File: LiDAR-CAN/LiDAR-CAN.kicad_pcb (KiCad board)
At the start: 4 copper layers, 60 x 55 mm, 138 parts, among them J1 XT30(2+2), J2 XT30(2+2), J3 G7LX-A88S7-BP-G/Y, J4 XT30(2+2), J5 61300511121, SW1 RST, U1 LMR51430, U2 LMR51430, U3 W5500, U4 TCAN4550RGY, U5 STM32F401RBT6, Y1 25MHz, Y2 40MHz, Y3 25MHz

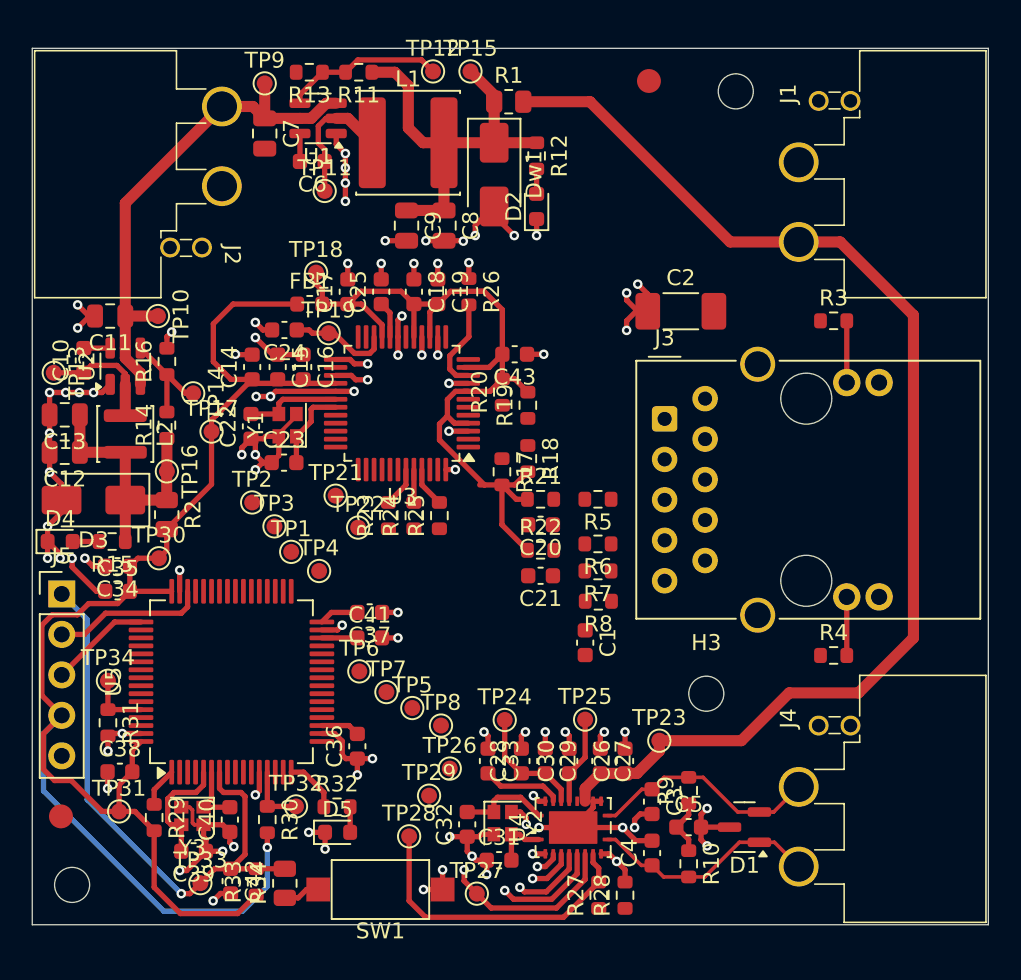
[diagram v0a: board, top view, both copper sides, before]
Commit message: Add Ethernet connector routing
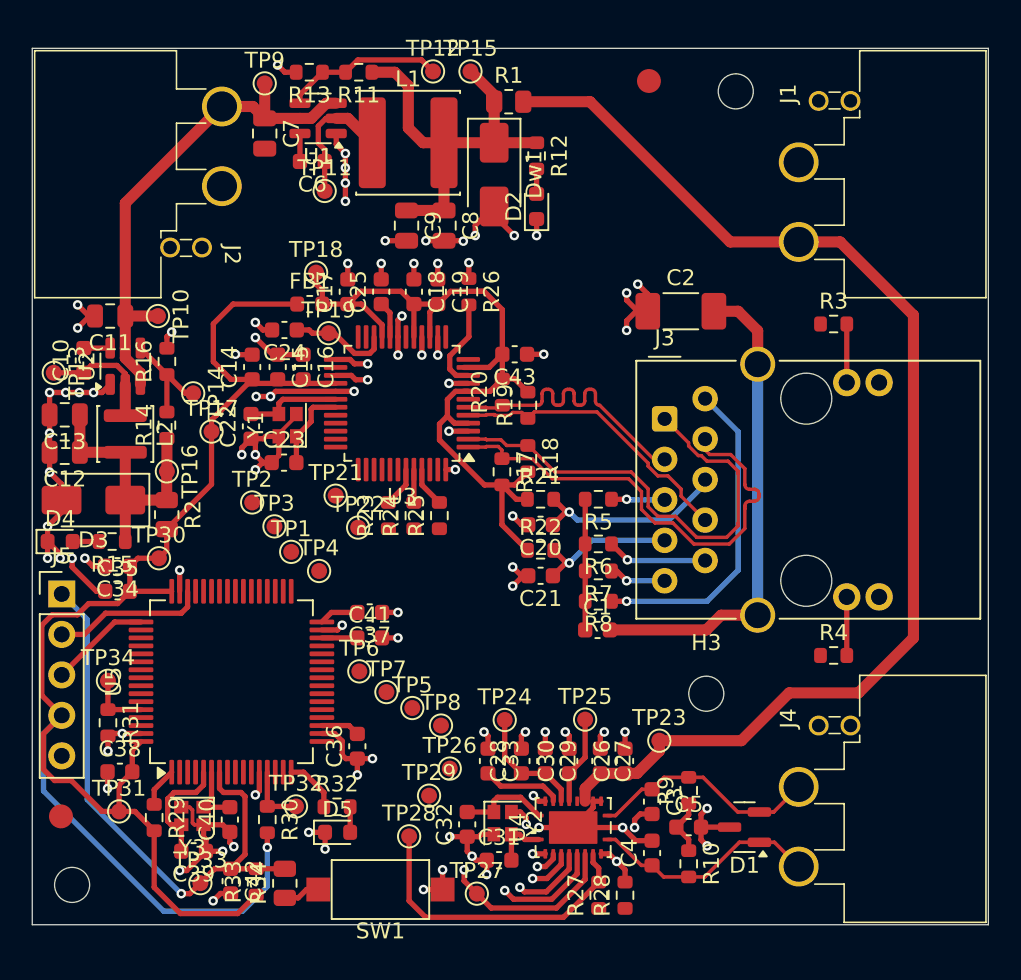
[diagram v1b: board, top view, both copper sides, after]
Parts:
- moved C1 1.11 mm to (155.5, 101.5), turned to 0 degrees
- moved R3 0.20 mm to (170.3, 82.3)
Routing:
- net CHASSIS_GND: track 0.00 -> 30.8 mm
- net /LiDAR Interface/TXP: track 0.00 -> 30.0 mm
- net /LiDAR Interface/TXN: track 0.00 -> 29.9 mm
- net Net-(J3-R4): track 0.00 -> 20.4 mm, vias 0 -> 1
- net /LiDAR Interface/RXN: track 0.00 -> 18.5 mm
- net /LiDAR Interface/RXP: track 0.00 -> 18.3 mm
- net /LiDAR Interface/TCT: track 0.00 -> 12.6 mm, vias 0 -> 1
- net /LiDAR Interface/RCT: track 0.00 -> 9.24 mm, vias 0 -> 1
- net Net-(C1-Pad1): track 0.00 -> 8.23 mm
- net Net-(J3-R2): track 0.00 -> 6.31 mm, vias 0 -> 1
- net GND: track 143.2 -> 148.2 mm, vias 82 -> 86
- net Net-(J3-R3): track 0.00 -> 3.59 mm, vias 0 -> 1
- net Net-(J3-R1): track 0.00 -> 3.35 mm, vias 0 -> 1

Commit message: Add SPI buses routing
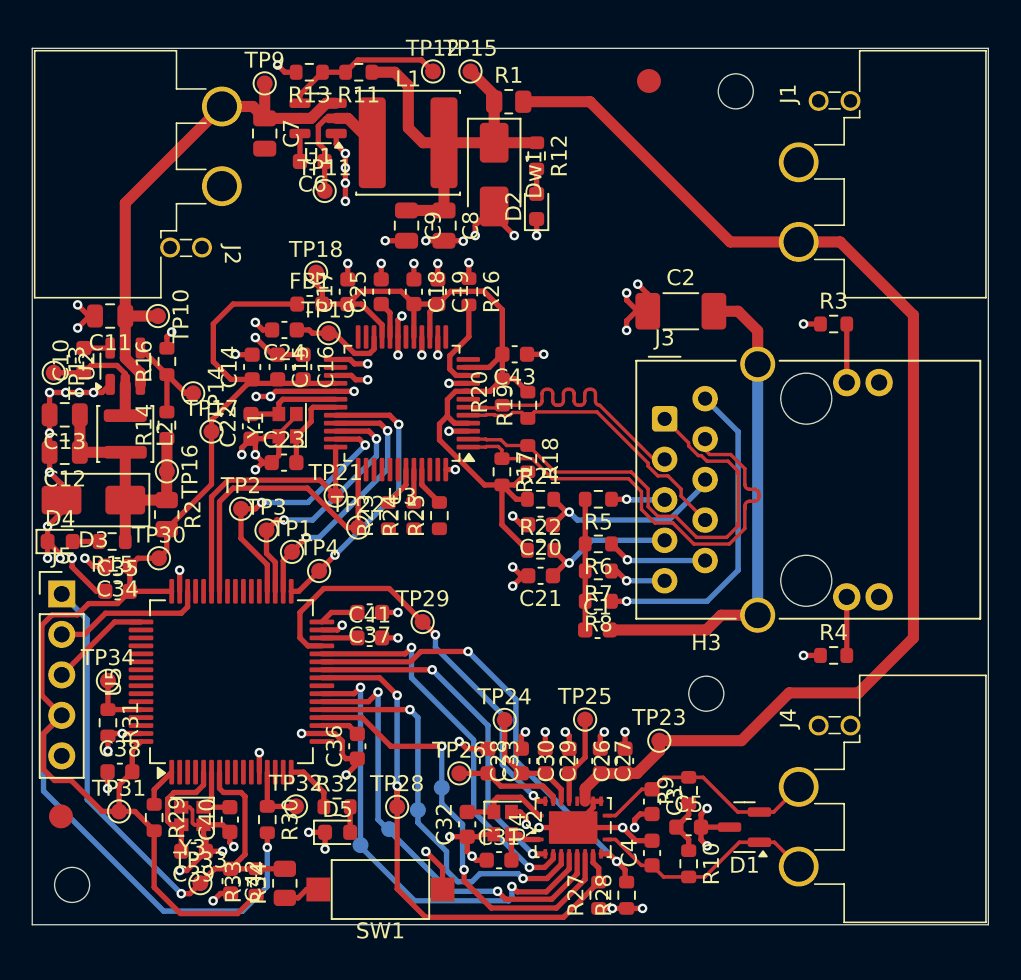
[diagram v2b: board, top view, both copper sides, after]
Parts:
- removed TP27: TestPoint, TestPoint:TestPoint_Pad_D1.0mm
- TP5, TP6, TP7, TP8: moved to B.Cu
- moved TP29 10.9 mm to (144.5, 101.0)
- moved TP6 10.9 mm to (140.6, 115.0), turned to 180 degrees
- moved TP7 8.60 mm to (142.4, 114.0), turned to 180 degrees
- moved TP5 6.41 mm to (144.2, 112.8), turned to 180 degrees
- moved TP8 3.90 mm to (145.7, 111.4), turned to 180 degrees
- moved TP28 2.00 mm to (142.9, 112.6)
- moved TP2 0.81 mm to (133.1, 93.9)
- moved TP26 0.67 mm to (146.8, 110.5)
- moved TP3 0.56 mm to (134.7, 95.2)
- moved R28 0.10 mm to (157.3, 118.2)
- moved TP1 0.05 mm to (136.3, 96.6)
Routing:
- net /CAN Interface/GPIO2: track 2.69 -> 29.2 mm, vias 1 -> 2
- net /CAN Interface/RST: track 0.89 -> 27.0 mm, vias 1 -> 2
- net /CAN Interface/SDI: track 4.76 -> 29.6 mm, vias 1 -> 2
- net /CAN Interface/GPIO1: track 1.51 -> 24.7 mm, vias 1 -> 2
- net /CAN Interface/SCLK: track 2.82 -> 25.4 mm, vias 1 -> 2
- net /CAN Interface/SDO: track 6.69 -> 28.3 mm, vias 1 -> 2
- net /CAN Interface/~{WKRQ}: track 0.79 -> 21.9 mm, vias 1 -> 2
- net /LiDAR Interface/~{RST}: track 0.00 -> 19.3 mm
- net /LiDAR Interface/~{SCS}: track 0.00 -> 17.7 mm, vias 0 -> 2
- net /LiDAR Interface/~{INT}: track 0.00 -> 17.6 mm
- net /LiDAR Interface/MOSI: track 0.00 -> 17.3 mm, vias 0 -> 2
- net /LiDAR Interface/MISO: track 0.00 -> 16.7 mm, vias 0 -> 2
- net /LiDAR Interface/SCLK: track 0.00 -> 16.7 mm, vias 0 -> 2
- net /CAN Interface/~{CS}: track 11.3 -> 27.9 mm, vias 1 -> 2
- net /CAN Interface/~{INT}: track 19.2 -> 34.9 mm, vias 0 -> 2
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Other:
- board text added: "FABRICATION DRAWING"

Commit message: Complete routing and all nets
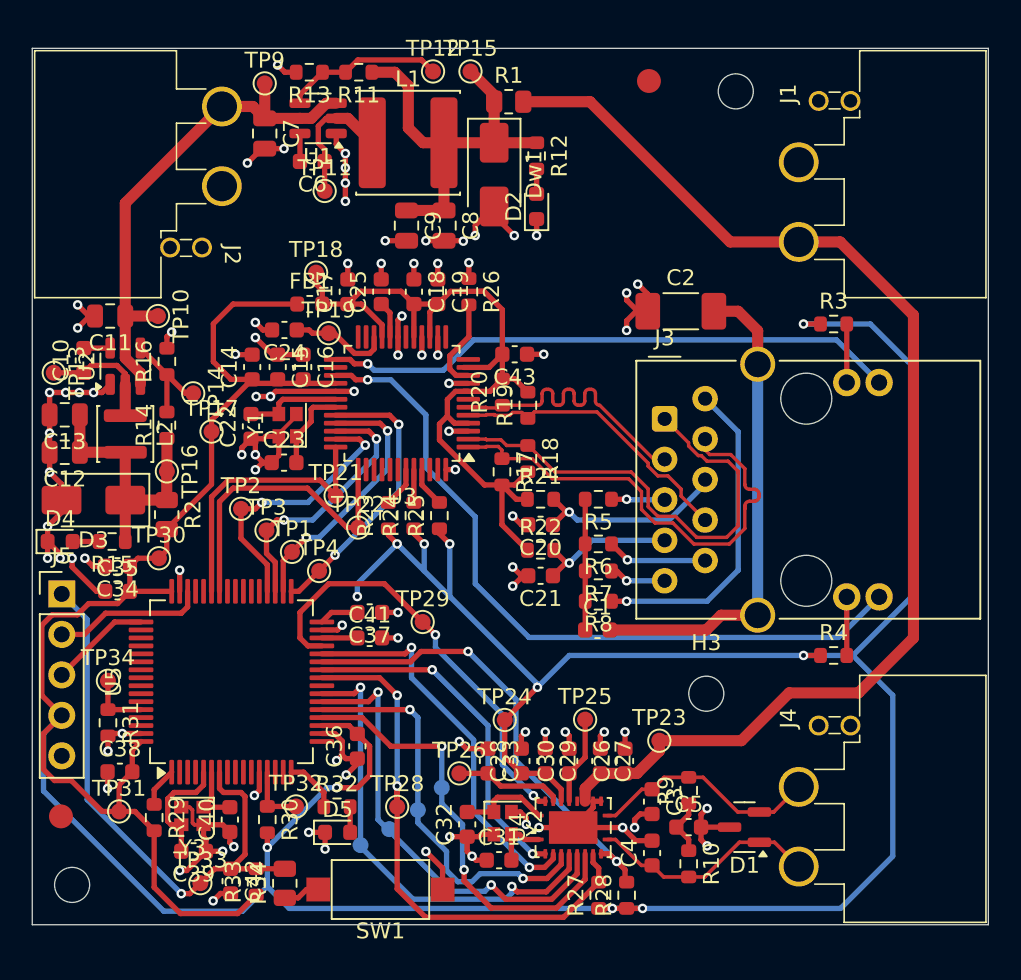
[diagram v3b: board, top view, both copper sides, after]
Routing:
- net +3.3V: track 120.4 -> 263.3 mm, vias 5 -> 11
- net /LiDAR Interface/ACTLED: track 2.13 -> 46.4 mm
- net /LiDAR Interface/LINKLED: track 2.13 -> 36.3 mm
- net GND: track 148.8 -> 151.4 mm, vias 84 -> 86

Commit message: Add new silkscreen annotation
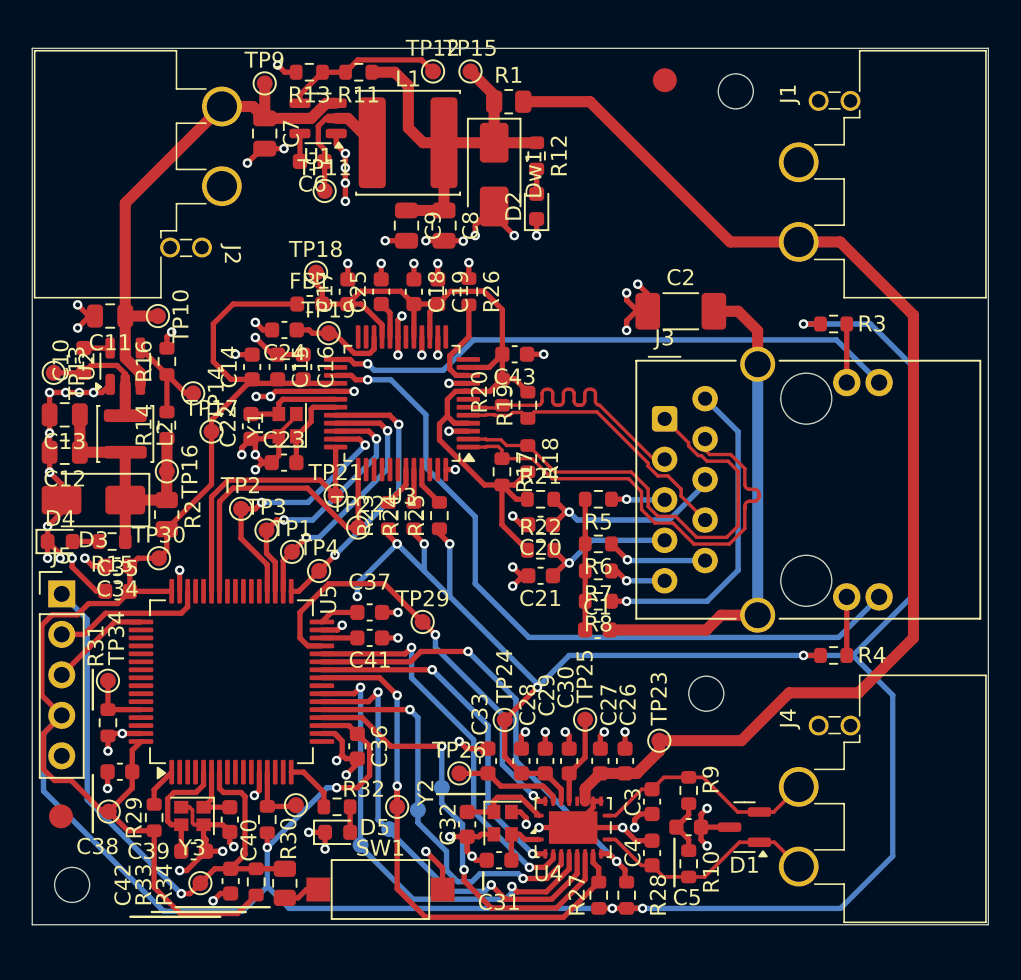
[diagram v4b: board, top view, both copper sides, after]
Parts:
- moved FID1 1.00 mm to (159.7, 67.0)
- moved TP31 0.65 mm to (124.8, 112.9)
- moved TP32 0.08 mm to (136.6, 112.5)
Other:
- board text added: "CAN P CAN L"
- board text added: "GND +12V"
- board text added: "RST SWDIO SWCLK +3.3V GND"
- board text added: "VIN GND"

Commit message: Complete silkscreen annotation
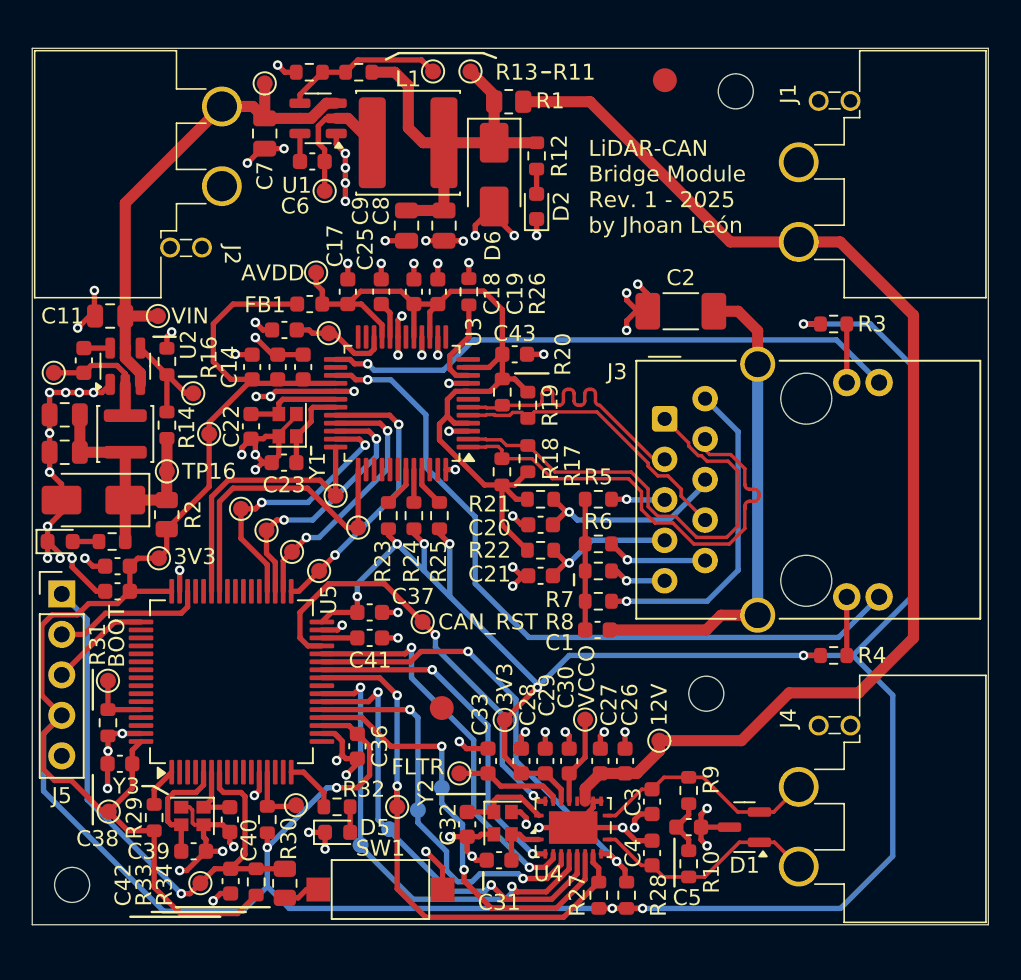
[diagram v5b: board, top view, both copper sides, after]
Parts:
- moved FID2 24.8 mm to (145.7, 106.4)
- moved C38 0.50 mm to (125.5, 109.9)
- moved 3V3 0.21 mm to (131.1, 89.2)
- turned SW_12V to 180 degrees
- renumbered TP23 to 12V, TP15 to 12V, TP19 to 1V20, TP31 to 3V3, TP24 to 3V3, TP17 to 3V3, TP30 to 3V3, TP18 to AVDD, TP34 to BOOT, TP8 to CAN_CS, TP28 to CAN_INT, TP7 to CAN_MISO, TP6 to CAN_MOSI, TP29 to CAN_RST, TP5 to CAN_SCLK, Dw1 to D6, TP21 to ETH_INT, TP3 to ETH_MISO, TP2 to ETH_MOSI, TP22 to ETH_RST, TP1 to ETH_SCLK, TP4 to ETH_SCS, TP12 to FB_12V, TP14 to FB_3V3, TP26 to FLTR, TP33 to MCU_RST, TP11 to SW_12V, TP13 to SW_3V3, TP25 to VCCO, TP10 to VIN, TP9 to VIN, TP32 to VREF+
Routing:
- net GND: track 151.4 -> 152.9 mm
- net +3.3V: track 263.5 -> 264.5 mm
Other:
- board text added: "ETHERNET 10/100BASE"
- board text added: "GND 12V"
- board text added: "LiDAR-CAN Bridge Module Rev. 1 - 2025 by Jhoan León"
- board text removed: "GND +12V"

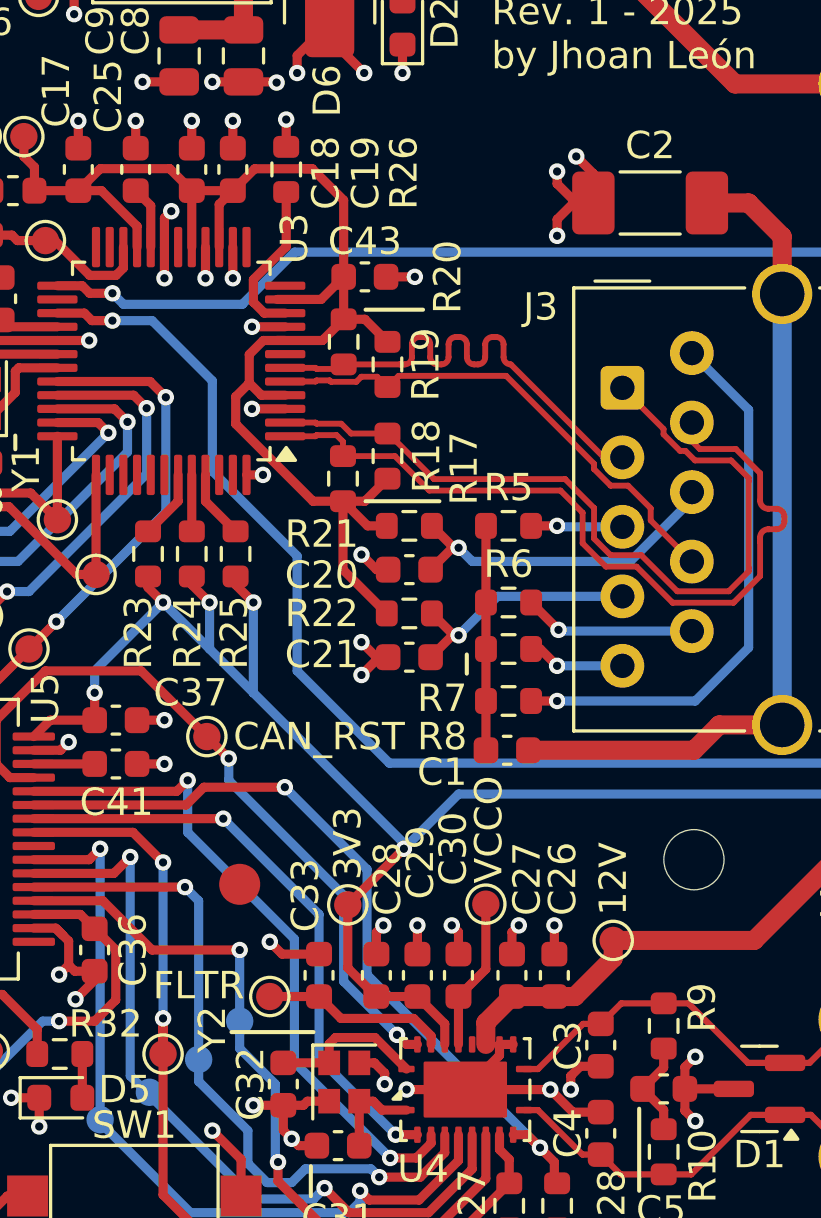
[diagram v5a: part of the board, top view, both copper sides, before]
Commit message: Feature schematic revision 2
Main changes related to connection wires for easy layout and minor components adjustments from Rev 1
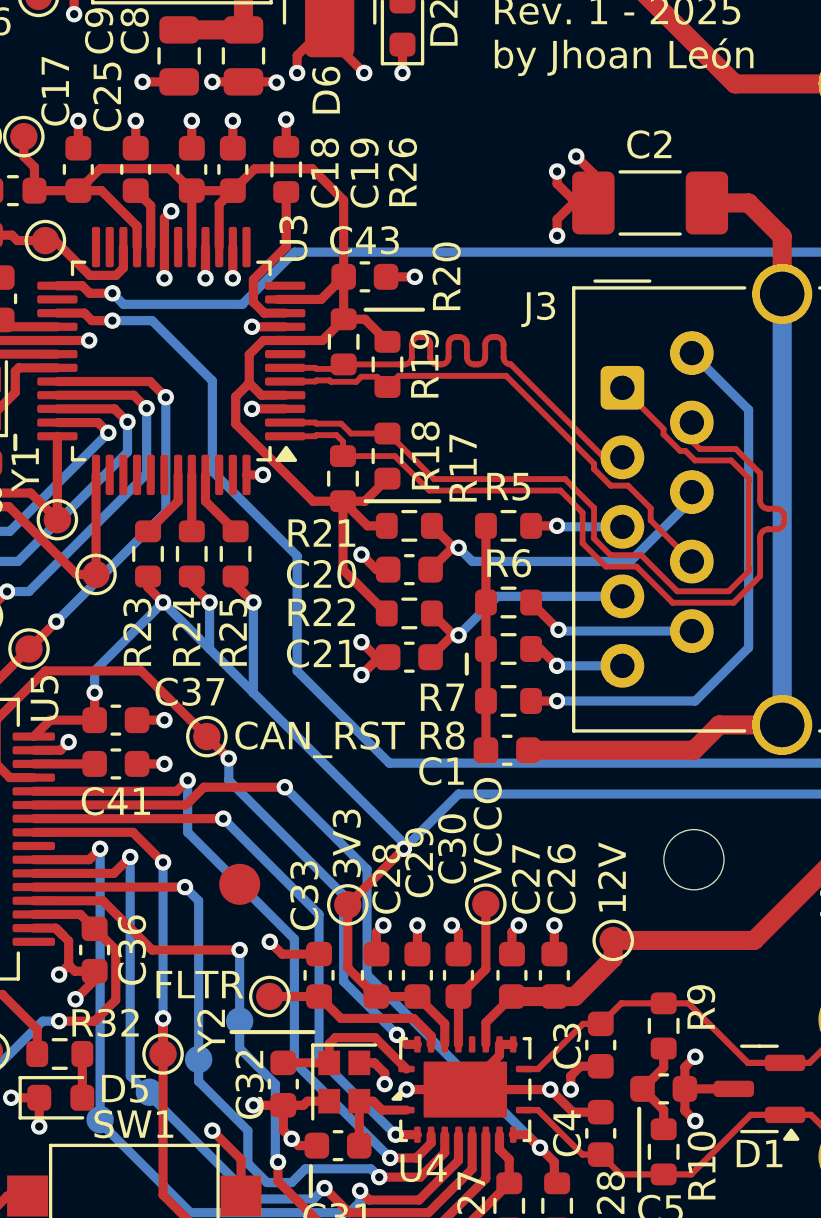
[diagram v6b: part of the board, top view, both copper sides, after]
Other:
- board text added: "0.1270 mm / 0.1270 mm"
- board text added: "0.2000 mm"
- board text added: "1.5960 mm"
- board text added: "4"
- board text added: "60.0000 mm x 55.0000 mm"
- board text added: "BOARD CHARACTERISTICS"
- board text added: "Board Thickness:"
- board text added: "Board overall dimensions:"
- board text added: "Castellated pads:"
- board text added: "Copper Finish:"
- board text added: "Copper Layer Count:"
- board text added: "Edge card connectors:"
- board text added: "HAL SnPb"
- board text added: "Impedance Control:"
- board text added: "Min hole diameter:"
- board text added: "Min track/spacing:"
- board text added: "No"
- board text added: "Plated Board Edge:"
- board text added: "TOP LAYER"
- board text added: "Yes"
- board text removed: "TOP = SIG/PWR IN1 = GND IN2 = GND BOTTOM = SIG/PWR"

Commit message: Feature layout revision 1
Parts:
- added REF**: ESD-Logo_6.6x6mm_SilkScreen, Symbol:ESD-Logo_6.6x6mm_SilkScreen, B.Cu at (135.2, 103.8)
- added REF**: WEEE-Logo_4.2x6mm_SilkScreen, Symbol:WEEE-Logo_4.2x6mm_SilkScreen, B.Cu at (159.5, 73.8)
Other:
- board text added: "CAN BUS"
- board text added: "DRILL MAP AND TABLE"
- board text added: "MID-160 POWER"
- board text added: "POWER INPUT"
- board text added: "STACK-UP TABLE (JLC041611-7628)"
- board text removed: "STACK-UP LAYER (JLC041611-7628)"
